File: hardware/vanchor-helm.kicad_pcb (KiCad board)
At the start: 2 copper layers, 150 x 120 mm, 70 parts, among them J1 PI_40PIN_STACK, J10 DISP PWR 5V, J11 AS5600, J12 PICO UTIL, J13 THRUST DRV, J14 BUCK 5V, J16 BATT 12V, J2 PI_BREAKOUT, J22 SERVO MOTOR, J3 UART0 ttyAMA0, J4 UART2 ttyAMA2, J5 UART3 ttyAMA3, J6 UART4 ttyAMA4, J7 UART5 ttyAMA5, J8 I2C1 spare, J9 FAN 5V, Q1 IRF9540N, U1 Pico 2, U7 BTN8982TA, U8 BTN8982TA

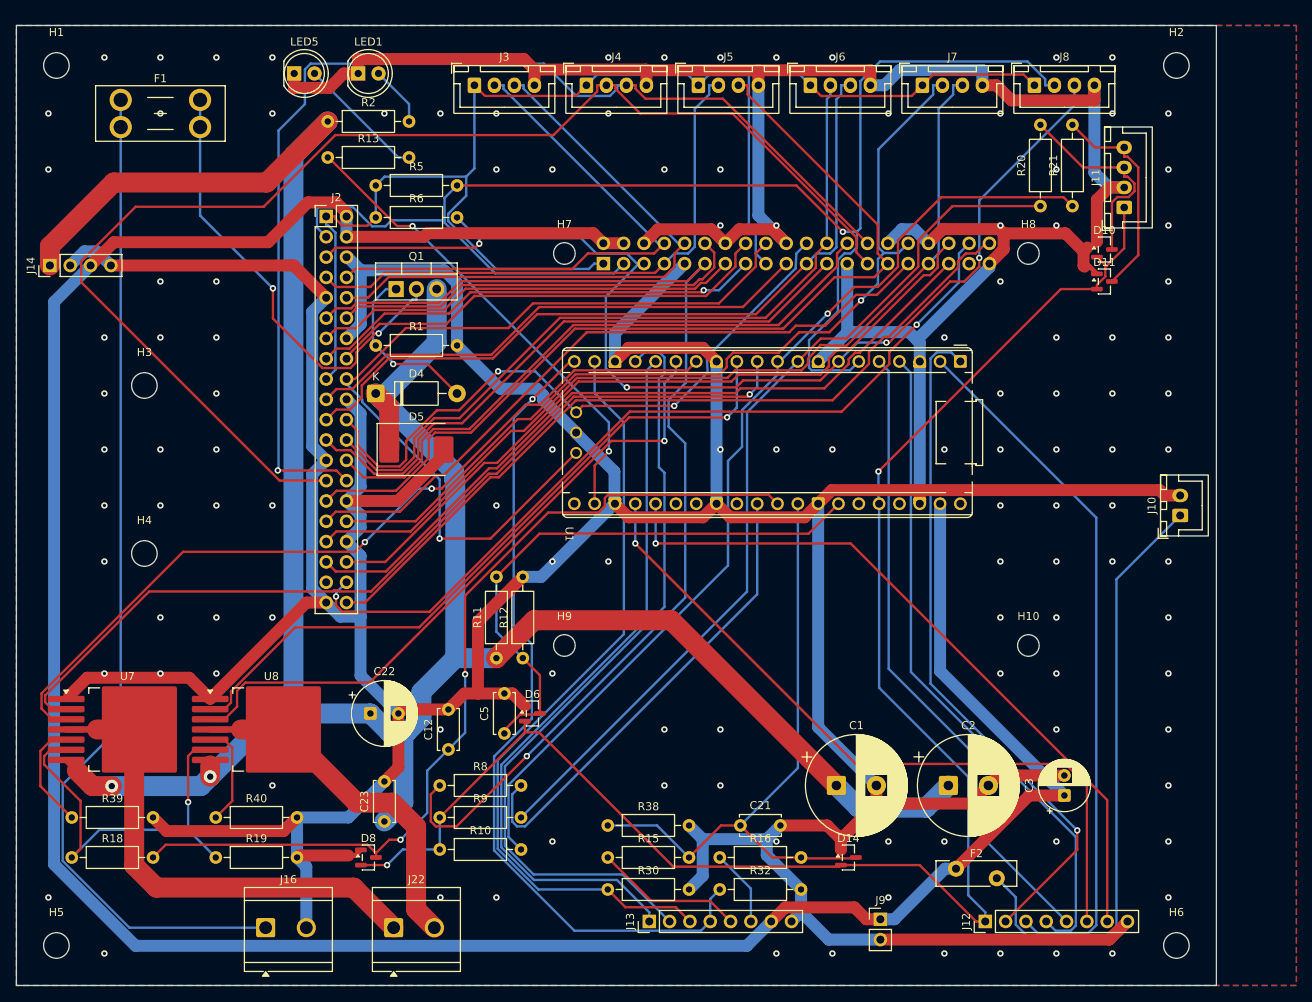
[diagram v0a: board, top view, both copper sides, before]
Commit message: feat: v4 Orange Pi Zero 3 carrier — 125x95mm, 26-pin socket, module-on-top, DRC clean
Co-Authored-By: Claude Fable 5 <noreply@anthropic.com>
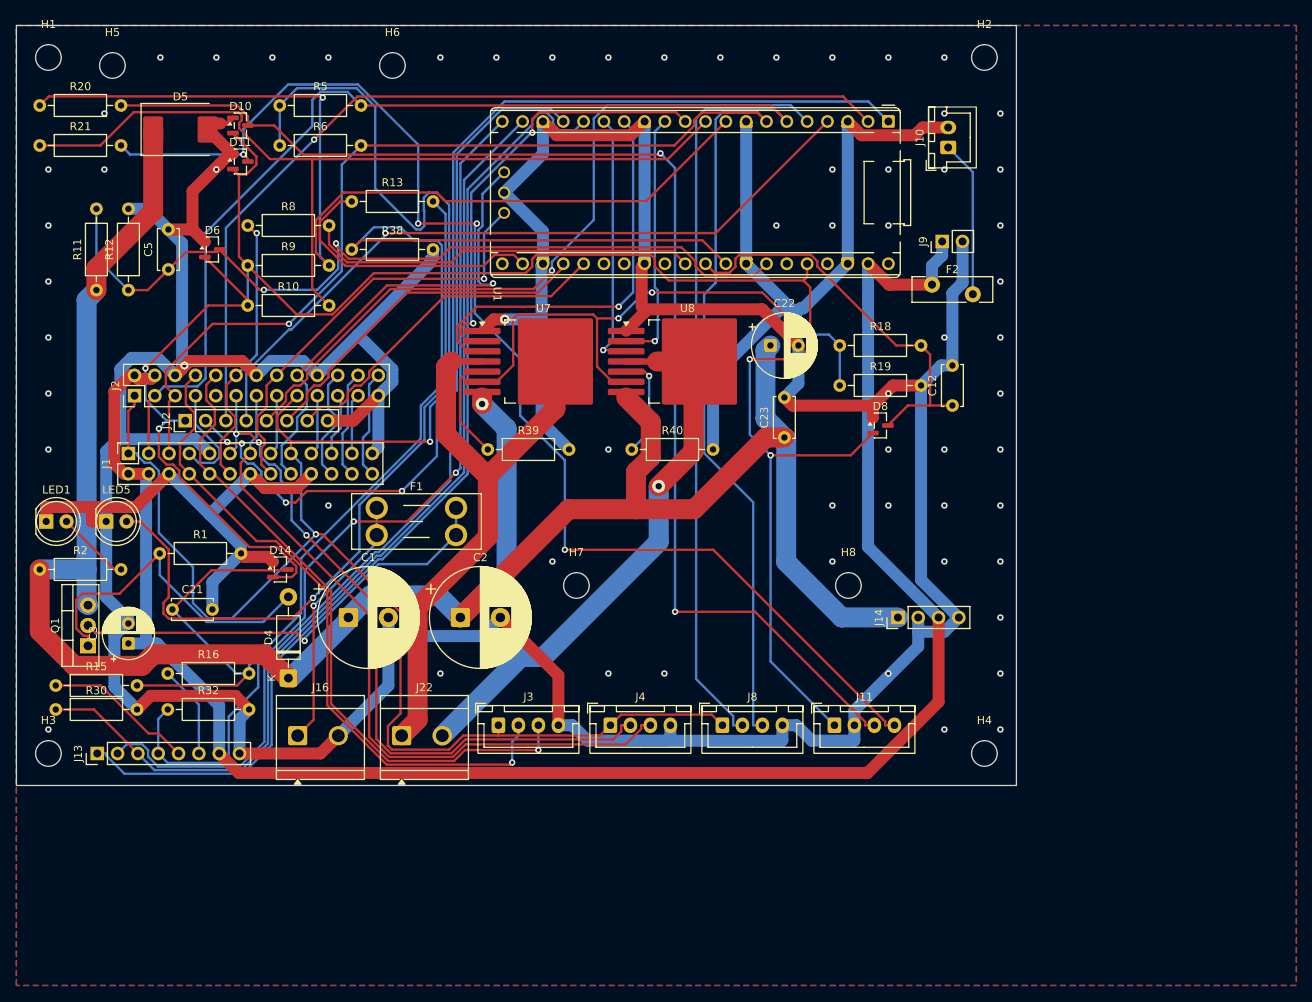
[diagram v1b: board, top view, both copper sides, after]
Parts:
- removed H10, H9: MountingHole_2.7mm_M2.5, MountingHole_2.7mm_M2.5
- removed J5: UART3 ttyAMA3, JST_XH_B4B-XH-A_1x04_P2.50mm_Vertical
- removed J6: UART4 ttyAMA4, JST_XH_B4B-XH-A_1x04_P2.50mm_Vertical
- removed J7: UART5 ttyAMA5, JST_XH_B4B-XH-A_1x04_P2.50mm_Vertical
- H7, H8: value MountingHole_2.7mm_M2.5 -> MountingHole_3.2mm_M3; footprint MountingHole_2.7mm_M2.5 -> MountingHole_3.2mm_M3
- J1: value PI_40PIN_STACK -> OPI_Z3_26PIN; footprint PinSocket_2x20_P2.54mm_Vertical -> PinSocket_2x13_P2.54mm_Vertical; moved to F.Cu
- J10: value DISP PWR 5V -> AUX 5V (screen)
- J2: value PI_BREAKOUT -> OPI_BREAKOUT; footprint PinHeader_2x20_P2.54mm_Vertical -> PinHeader_2x13_P2.54mm_Vertical
- J3: value UART0 ttyAMA0 -> UART5 ttyAS5
- J4: value UART2 ttyAMA2 -> UART2 ttyAS2
- J8: value I2C1 spare -> I2C3 spare
- moved H6 147.3 mm to (67.0, 25.0)
- moved R21 129.3 mm to (22.9, 35.0), turned to 0 degrees
- moved R20 125.7 mm to (22.9, 30.0), turned to 0 degrees
- moved C3 118.5 mm to (34.0, 97.2)
- moved J12 118.0 mm to (41.1, 69.4)
- moved R18 115.4 mm to (122.9, 60.0)
- moved J14 114.8 mm to (130.2, 94.0)
- moved H5 110.2 mm to (32.0, 25.0)
- moved D10 109.1 mm to (48.0, 32.5)
- moved D11 109.0 mm to (48.0, 37.0)
- moved H4 107.9 mm to (141.0, 111.0)
- moved R19 97.8 mm to (122.9, 65.0)
- moved J8 89.0 mm to (108.2, 107.5)
- moved J9 85.1 mm to (135.7, 47.0), turned to 90 degrees
- moved D8 83.7 mm to (128.0, 70.0)
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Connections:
- net PI_GPIO10 renamed OPI_MOSI
- net PI_GPIO11 renamed OPI_SCLK
- net PI_GPIO22 renamed OPI_PC8
- net PI_GPIO7 renamed OPI_PC10
- net UART3_TX renamed OPI_PC9
- net UART4_RX renamed OPI_MISO
- net UART4_TX renamed OPI_CS
- J1 pad 10: UART0_RX -> UART5_RX
- J1 pad 11: PI_PICO_RUN -> UART2_TX
- J1 pad 12: PI_GPIO18 -> PI_PICO_RUN
- J1 pad 13: PI_GPIO27 -> UART2_RX
- J1 pad 16: PI_GPIO23 -> PI_GPIO24
- J1 pad 18: PI_GPIO24 -> PI_GPIO25
- J1 pad 22: PI_GPIO25 -> OPI_PC7
- J1 pad 8: UART0_TX -> UART5_TX
- J2 pad 10: UART0_RX -> UART5_RX
- J2 pad 11: PI_PICO_RUN -> UART2_TX
- J2 pad 12: PI_GPIO18 -> PI_PICO_RUN
- J2 pad 13: PI_GPIO27 -> UART2_RX
- J2 pad 16: PI_GPIO23 -> PI_GPIO24
- J2 pad 18: PI_GPIO24 -> PI_GPIO25
- J2 pad 22: PI_GPIO25 -> OPI_PC7
- J2 pad 8: UART0_TX -> UART5_TX
- J3 pad 2: UART0_TX -> UART5_TX
- J3 pad 3: UART0_RX -> UART5_RX
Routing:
- net GND: track 917.9 -> 690.5 mm, vias 118 -> 62
- net /servo/ENC_SDA_J: track 25.7 -> 159.8 mm, vias 0 -> 2
- net /servo/ENC_SCL_J: track 26.7 -> 160.6 mm, vias 0 -> 4
- net UART3_RX: track 114.6 -> 0.00 mm
- net PI_PICO_RUN: track 143.5 -> 34.8 mm
- net PI_GPIO20: track 105.0 -> 0.00 mm, vias 2 -> 0
- net +5V: track 333.3 -> 230.0 mm
- net PI_GPIO21: track 100.3 -> 0.00 mm
- net PI_GPIO19: track 94.6 -> 0.00 mm
- net /power/BATT_IN: track 127.0 -> 32.6 mm, vias 0 -> 1
- net PI_GPIO16: track 93.3 -> 0.00 mm
- net THR_IS: track 79.3 -> 169.3 mm
- net OPI_MISO: track 95.2 -> 7.85 mm
- net PI_GPIO6: track 86.1 -> 0.00 mm
- net OPI_CS: track 95.6 -> 13.6 mm
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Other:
- board size 150 x 120 mm -> 125 x 95 mm

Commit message: feat: v4.1 — J1 male header for 26-way IDC ribbon (pre-soldered Zero 3), J1.14/J2.9 NC by design, clearance 0.14; DRC clean
Co-Authored-By: Claude Fable 5 <noreply@anthropic.com>
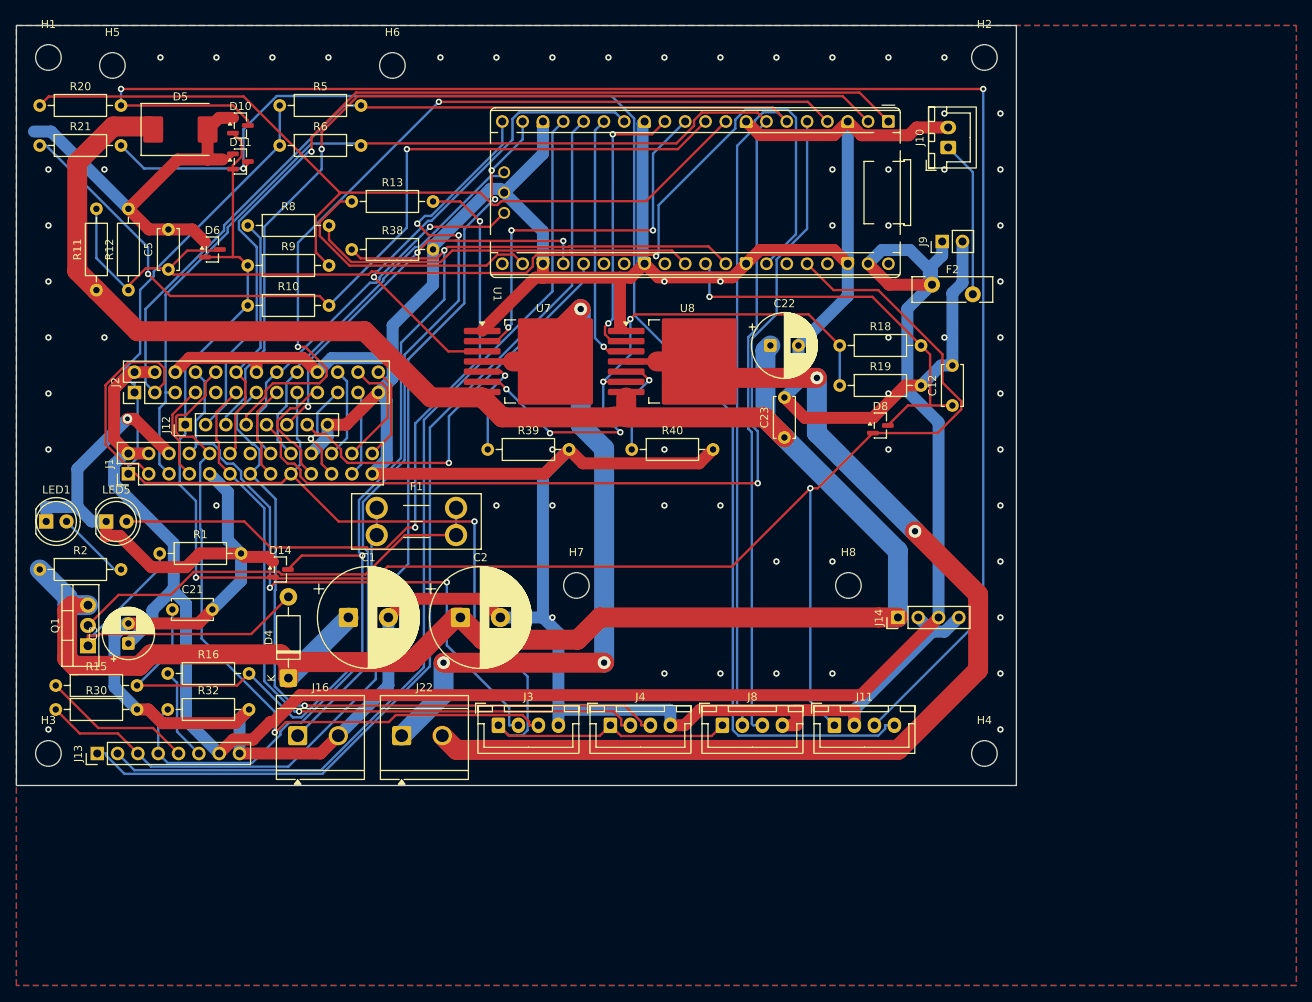
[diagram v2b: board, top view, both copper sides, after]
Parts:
- J1: footprint PinSocket_2x13_P2.54mm_Vertical -> PinHeader_2x13_P2.54mm_Vertical
- moved J1 2.54 mm to (34.0, 76.0)
- moved J12 0.50 mm to (41.1, 69.9)
- moved J2 0.40 mm to (34.8, 65.9)
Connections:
- J1 pad 14: GND -> (no net)
- J2 pad 9: GND -> (no net)
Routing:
- net SERVO_B: track 70.9 -> 141.4 mm, vias 1 -> 2
- net 3V3_PI: track 242.2 -> 177.1 mm, vias 2 -> 1
- net /servo/ENC_SDA_J: track 159.8 -> 212.3 mm
- net VBAT_SENSE: track 104.6 -> 138.4 mm, vias 2 -> 1
- net VIN: track 282.0 -> 306.9 mm, vias 1 -> 0
- net +3V3: track 252.9 -> 230.4 mm, vias 4 -> 2
- net GND: track 690.5 -> 668.6 mm
- net PICO_GP3: track 93.9 -> 114.6 mm
- net SERVO_A: track 75.4 -> 93.8 mm, vias 0 -> 3
- net /servo/ENC_SCL_J: track 160.6 -> 177.0 mm, vias 4 -> 1
- net PICO_GP2: track 91.9 -> 106.8 mm, vias 1 -> 2
- net PICO_GP0: track 134.1 -> 119.4 mm, vias 4 -> 1
- net ENC_SDA: track 121.1 -> 107.2 mm, vias 1 -> 0
- net PI_GPIO25: track 60.9 -> 48.6 mm, vias 1 -> 0
- net THR_IS: track 169.3 -> 159.7 mm, vias 0 -> 2
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
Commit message: fix: F2 footprint MF-RG300 (was oversized RG400, body offset); feat: readable 2-page schematic (carrier/control merged specs)
Co-Authored-By: Claude Fable 5 <noreply@anthropic.com>
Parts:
- F2: footprint Fuse_Bourns_MF-RG400 -> Fuse_Bourns_MF-RG300
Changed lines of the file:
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@@
 		)
 	)
-	(footprint "Fuse_Bourns_MF-RG400"
-		(layer "F.Cu")
-		(at 134.45 52.4)
-		(descr "PTC Resettable Fuse, Ihold = 4.0A, Itrip=6.8A, http://www.bourns.com/docs/Product-Datasheets/mfrg.pdf")
-		(tags "ptc resettable fuse polyfuse THT")
-		(property "Reference" "F2"
-			(at 2.55 -1.9 0)
-			(layer "F.SilkS")
-			(effects
-				(font
-					(size 1 1)
-					(thickness 0.15)
-				)
-			)
-		)
-		(property "Value" "MF-R200 2A"
-			(at 2.55 3.1 0)
-			(layer "F.Fab")
-			(effects
-				(font
-					(size 1 1)
-					(thickness 0.15)
-				)
-			)
-		)
-		(property "Datasheet" ""
-			(at 0 0 0)
-			(layer "F.Fab")
-			(hide yes)
-			(effects
-				(font
-					(size 1.27 1.27)
-				)
-			)
-		)
-		(property "Description" ""
-			(at 0 0 0)
-			(layer "F.Fab")
-			(hide yes)
-			(effects
-				(font
-					(size 1.27 1.27)
-				)
-			)
-		)
-		(attr through_hole)
-		(duplicate_pad_numbers_are_jumpers no)
-		(fp_line
-			(start -2.5 -1)
-			(end -0.838 -1)
-			(stroke
-				(width 0.12)
-				(type solid)
-			)
-			(layer "F.SilkS")
-		)
-		(fp_line
-			(start -2.5 2.2)
-			(end -2.5 -1)
-			(stroke
-				(width 0.12)
-				(type solid)
-			)
-			(layer "F.SilkS")
-		)
-		(fp_line
-			(start 0.838 -1)
-			(end 7.6 -1)
-			(stroke
-				(width 0.12)
-				(type solid)
-			)
-			(layer "F.SilkS")
-		)
-		(fp_line
-			(start 4.262 2.2)
-			(end -2.5 2.2)
-			(stroke
-				(width 0.12)
-				(type solid)
-			)
-			(layer "F.SilkS")
-		)
-		(fp_line
-			(start 7.6 -1)
-			(end 7.6 2.2)
-			(stroke
-				(width 0.12)
-				(type solid)
-			)
-			(layer "F.SilkS")
-		)
-		(fp_line
-			(start 7.6 2.2)
-			(end 5.938 2.2)
-			(stroke
-				(width 0.12)
-				(type solid)
-			)
-			(layer "F.SilkS")
-		)
-		(fp_rect
-			(start -2.65 -1.15)
-			(end 7.75 2.35)
-			(stroke
-				(width 0.05)
-				(type solid)
-			)
-			(fill no)
-			(layer "F.CrtYd")
-		)
-		(fp_rect
-			(start -2.4 -0.9)
-			(end 7.5 2.1)
-			(stroke
-				(width 0.1)
-				(type solid)
-			)
-			(fill no)
-			(layer "F.Fab")
-		)
-		(fp_text user "${REFERENCE}"
-			(at 2.55 0.6 0)
-			(layer "F.Fab")
-			(effects
-				(font
-					(size 1 1)
-					(thickness 0.15)
-				)
-			)
-		)
-		(pad "1" thru_hole circle
-			(at 0 0)
-			(size 2.01 2.01)
-			(drill 1.01)
-			(layers "*.Cu" "*.Mask")
-			(remove_unused_layers no)
-			(net "+5V")
-		)
-		(pad "2" thru_hole circle
-			(at 5.1 1.2)
-			(size 2.01 2.01)
-			(drill 1.01)
-			(layers "*.Cu" "*.Mask")
-			(remove_unused_layers no)
-			(net "DISP_5V")
-		)
-		(embedded_fonts no)
-		(model "${KICAD9_3DMODEL_DIR}/Fuse.3dshapes/Fuse_Bourns_MF-RG400.step"
-			(offset
-				(xyz 0 0 0)
-			)
-			(scale
-				(xyz 1 1 1)
-			)
-			(rotate
-				(xyz 0 0 0)
-			)
-		)
-	)
 	(footprint "JST_XH_B4B-XH-A_1x04_P2.50mm_Vertical"
 		(layer "F.Cu")
@@
 			(offset
 				(xyz 0 0 0)
+			)
+			(scale
+				(xyz 1 1 1)
+			)
+			(rotate
+				(xyz 0 0 0)
+			)
+		)
+	)
+	(footprint "Fuse_Bourns_MF-RG300"
+		(layer "F.Cu")
+		(at 134.45 52.4)
+		(descr "PTC Resettable Fuse, Ihold = 3.0A, Itrip=5.1A, http://www.bourns.com/docs/Product-Datasheets/mfrg.pdf")
+		(tags "ptc resettable fuse polyfuse THT")
+		(property "Reference" "F2"
+			(at 2.55 -1.9 0)
+			(layer "F.SilkS")
+			(effects
+				(font
+					(size 1 1)
+					(thickness 0.15)
+				)
+			)
+		)
+		(property "Value" "MF-R200 2A"
+			(at 2.55 3.1 0)
+			(layer "F.Fab")
+			(effects
+				(font
+					(size 1 1)
+					(thickness 0.15)
+				)
+			)
+		)
+		(property "Datasheet" ""
+			(at 0 0 0)
+			(layer "F.Fab")
+			(hide yes)
+			(effects
+				(font
+					(size 1.27 1.27)
+				)
+			)
+		)
+		(property "Description" ""
+			(at 0 0 0)
+			(layer "F.Fab")
+			(hide yes)
+			(effects
+				(font
+					(size 1.27 1.27)
+				)
+			)
+		)
+		(attr through_hole)
+		(duplicate_pad_numbers_are_jumpers no)
+		(fp_line
+			(start -1.1 -1)
+			(end -0.838 -1)
+			(stroke
+				(width 0.12)
+				(type solid)
+			)
+			(layer "F.SilkS")
+		)
+		(fp_line
+			(start -1.1 -0.702)
+			(end -1.1 -1)
+			(stroke
+				(width 0.12)
+				(type solid)
+			)
+			(layer "F.SilkS")
+		)
+		(fp_line
+			(start -1.1 2.2)
+			(end -1.1 0.702)
+			(stroke
+				(width 0.12)
+				(type solid)
+			)
+			(layer "F.SilkS")
+		)
+		(fp_line
+			(start 0.838 -1)
+			(end 6.2 -1)
+			(stroke
+				(width 0.12)
+				(type solid)
+			)
+			(layer "F.SilkS")
+		)
+		(fp_line
+			(start 4.262 2.2)
+			(end -1.1 2.2)
+			(stroke
+				(width 0.12)
+				(type solid)
+			)
+			(layer "F.SilkS")
+		)
+		(fp_line
+			(start 6.2 -1)
+			(end 6.2 0.498)
+			(stroke
+				(width 0.12)
+				(type solid)
+			)
+			(layer "F.SilkS")
+		)
+		(fp_line
+			(start 6.2 1.902)
+			(end 6.2 2.2)
+			(stroke
+				(width 0.12)
+				(type solid)
+			)
+			(layer "F.SilkS")
+		)
+		(fp_line
+			(start 6.2 2.2)
+			(end 5.938 2.2)
+			(stroke
+				(width 0.12)
+				(type solid)
+			)
+			(layer "F.SilkS")
+		)
+		(fp_rect
+			(start -1.25 -1.15)
+			(end 6.35 2.35)
+			(stroke
+				(width 0.05)
+				(type solid)
+			)
+			(fill no)
+			(layer "F.CrtYd")
+		)
+		(fp_rect
+			(start -1 -0.9)
+			(end 6.1 2.1)
+			(stroke
+				(width 0.1)
+				(type solid)
+			)
+			(fill no)
+			(layer "F.Fab")
+		)
+		(fp_text user "${REFERENCE}"
+			(at 2.55 0.6 0)
+			(layer "F.Fab")
+			(effects
+				(font
+					(size 1 1)
+					(thickness 0.15)
+				)
+			)
+		)
+		(pad "1" thru_hole circle
+			(at 0 0)
+			(size 2.01 2.01)
+			(drill 1.01)
+			(layers "*.Cu" "*.Mask")
+			(remove_unused_layers no)
+			(net "+5V")
+		)
+		(pad "2" thru_hole circle
+			(at 5.1 1.2)
+			(size 2.01 2.01)
+			(drill 1.01)
+			(layers "*.Cu" "*.Mask")
+			(remove_unused_layers no)
+			(net "DISP_5V")
+		)
+		(embedded_fonts no)
+		(model "${KICAD9_3DMODEL_DIR}/Fuse.3dshapes/Fuse_Bourns_MF-RG300.step"
+			(offset
+				(xyz 0 0 0)

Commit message: chore: F2 MF-R200 -> MF-R250 (2.5A hold, same footprint)
Co-Authored-By: Claude Fable 5 <noreply@anthropic.com>
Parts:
- F2: value MF-R200 2A -> MF-R250 2.5A
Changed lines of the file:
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@@
 			)
 		)
-		(property "Value" "MF-R200 2A"
+		(property "Value" "MF-R250 2.5A"
 			(at 2.55 3.1 0)
 			(layer "F.Fab")

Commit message: feat: silkscreen connection legends (connector purposes, J13 pin order, J14 pin labels, polarity marks)
Co-Authored-By: Claude Fable 5 <noreply@anthropic.com>
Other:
- board text added: "+"
- board text added: "-"
- board text added: "1"
- board text added: "5V"
- board text added: "AS5600"
- board text added: "AUX 5V"
- board text added: "BATT 12V"
- board text added: "BUCK 5V"
- board text added: "F1 10A"
- board text added: "FAN"
- board text added: "GND"
- board text added: "I2C3"
- board text added: "OPI ZERO 3 RIBBON"
- board text added: "RPWM LPWM REN LEN RIS LIS 5V GND"
- board text added: "SERVO"
- board text added: "THRUST DRV"
- board text added: "UART2"
- board text added: "UART5"
- board text added: "VIN"
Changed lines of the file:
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@@
 		(layer "Edge.Cuts")
+	)
+	(gr_text "RPWM LPWM REN LEN RIS LIS 5V GND"
+		(at 39 113.8 0)
+		(layer "F.SilkS")
+		(effects
+			(font
+				(size 0.8 0.8)
+				(thickness 0.13)
+			)
+		)
+	)
+	(gr_text "VIN"
+		(at 130.19 97.9 90)
+		(layer "F.SilkS")
+		(effects
+			(font
+				(size 0.8 0.8)
+				(thickness 0.13)
+			)
+		)
+	)
+	(gr_text "GND"
+		(at 132.73 97.9 90)
+		(layer "F.SilkS")
+		(effects
+			(font
+				(size 0.8 0.8)
+				(thickness 0.13)
+			)
+		)
+	)
+	(gr_text "5V"
+		(at 135.269999 97.9 90)
+		(layer "F.SilkS")
+		(effects
+			(font
+				(size 0.8 0.8)
+				(thickness 0.13)
+			)
+		)
+	)
+	(gr_text "GND"
+		(at 137.81 97.9 90)
+		(layer "F.SilkS")
+		(effects
+			(font
+				(size 0.8 0.8)
+				(thickness 0.13)
+			)
+		)
+	)
+	(gr_text "F1 10A"
+		(at 70 76.8 0)
+		(layer "F.SilkS")
+		(effects
+			(font
+				(size 0.9 0.9)
+				(thickness 0.15)
+			)
+		)
+	)
+	(gr_text "THRUST DRV"
+		(at 39 107.7 0)
+		(layer "F.SilkS")
+		(effects
+			(font
+				(size 1 1)
+				(thickness 0.15)
+			)
+		)
+	)
+	(gr_text "BATT 12V"
+		(at 57.7 101 0)
+		(layer "F.SilkS")
+		(effects
+			(font
+				(size 1 1)
+				(thickness 0.15)
+			)
+		)
+	)
+	(gr_text "SERVO"
+		(at 70.7 101 0)
+		(layer "F.SilkS")
+		(effects
+			(font
+				(size 1 1)
+				(thickness 0.15)
+			)
+		)
+	)
+	(gr_text "UART5"
+		(at 84 102.5 0)
+		(layer "F.SilkS")
+		(effects
+			(font
+				(size 1 1)
+				(thickness 0.15)
+			)
+		)
+	)
+	(gr_text "UART2"
+		(at 98 102.5 0)
+		(layer "F.SilkS")
+		(effects
+			(font
+				(size 1 1)
+				(thickness 0.15)
+			)
+		)
+	)
+	(gr_text "I2C3"
+		(at 112 102.5 0)
+		(layer "F.SilkS")
+		(effects
+			(font
+				(size 1 1)
+				(thickness 0.15)
+			)
+		)
+	)
+	(gr_text "AS5600"
+		(at 126 102.5 0)
+		(layer "F.SilkS")
+		(effects
+			(font
+				(size 1 1)
+				(thickness 0.15)
+			)
+		)
+	)
+	(gr_text "BUCK 5V"
+		(at 134 90.5 0)
+		(layer "F.SilkS")
+		(effects
+			(font
+				(size 1 1)
+				(thickness 0.15)
+			)
+		)
+	)
+	(gr_text "AUX 5V"
+		(at 142.9 34 90)
+		(layer "F.SilkS")
+		(effects
+			(font
+				(size 1 1)
+				(thickness 0.15)
+			)
+		)
+	)
+	(gr_text "FAN"
+		(at 142.9 47 90)
+		(layer "F.SilkS")
+		(effects
+			(font
+				(size 1 1)
+				(thickness 0.15)
+			)
+		)
+	)
+	(gr_text "1"
+		(at 31.5 78.8 0)
+		(layer "F.SilkS")
+		(effects
+			(font
+				(size 1 1)
+				(thickness 0.2)
+			)
+		)
+	)
+	(gr_text "OPI ZERO 3 RIBBON"
+		(at 49 79.6 0)
+		(layer "F.SilkS")
+		(effects
+			(font
+				(size 1.2 1.2)
+				(thickness 0.2)
+			)
+		)
+	)
+	(gr_text "+"
+		(at 55.16 105.8 0)
+		(layer "F.SilkS")
+		(effects
+			(font
+				(size 1.4 1.4)
+				(thickness 0.25)
+			)
+		)
+	)
+	(gr_text "-"
+		(at 60.24 105.8 0)
+		(layer "F.SilkS")
+		(effects
+			(font
+				(size 1.4 1.4)
+				(thickness 0.25)
+			)
+		)
 	)
 	(segment
